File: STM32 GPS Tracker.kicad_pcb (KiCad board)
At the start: 2 copper layers, 57 parts, among them J1 Screw_Terminal_01x02, J2 LEFT HEADER PINS, J3 693010020611, J4 RIGHT HEADER PINS, Q1 AO3407A, SW1 SW_Push, SW2 SW_Push, U1 SIM808, U2 TPS5430DDA, U3 SMF05CT1G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

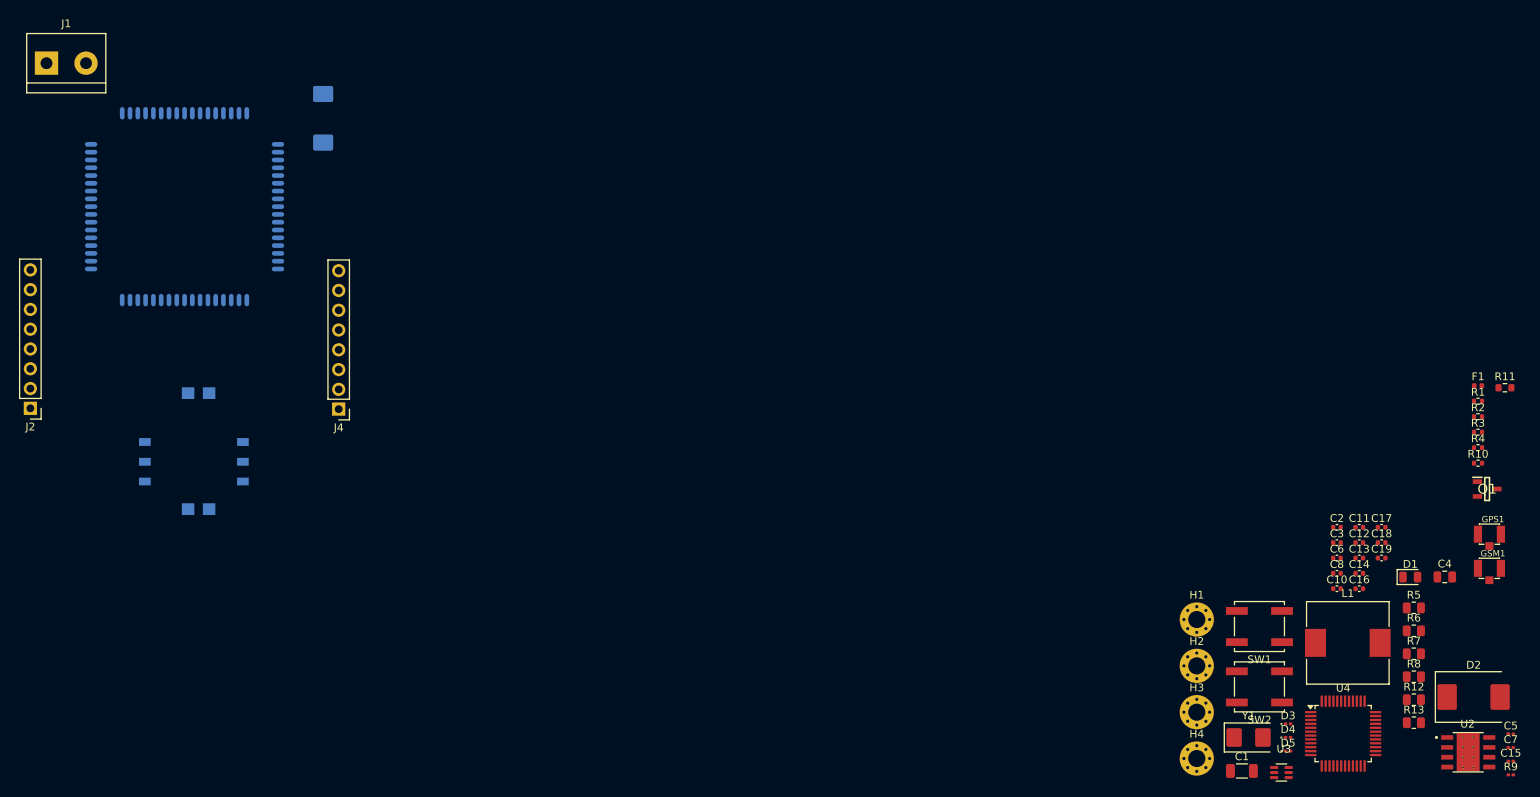
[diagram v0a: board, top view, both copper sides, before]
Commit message: Proper placing and edge cuts done for the Footprints
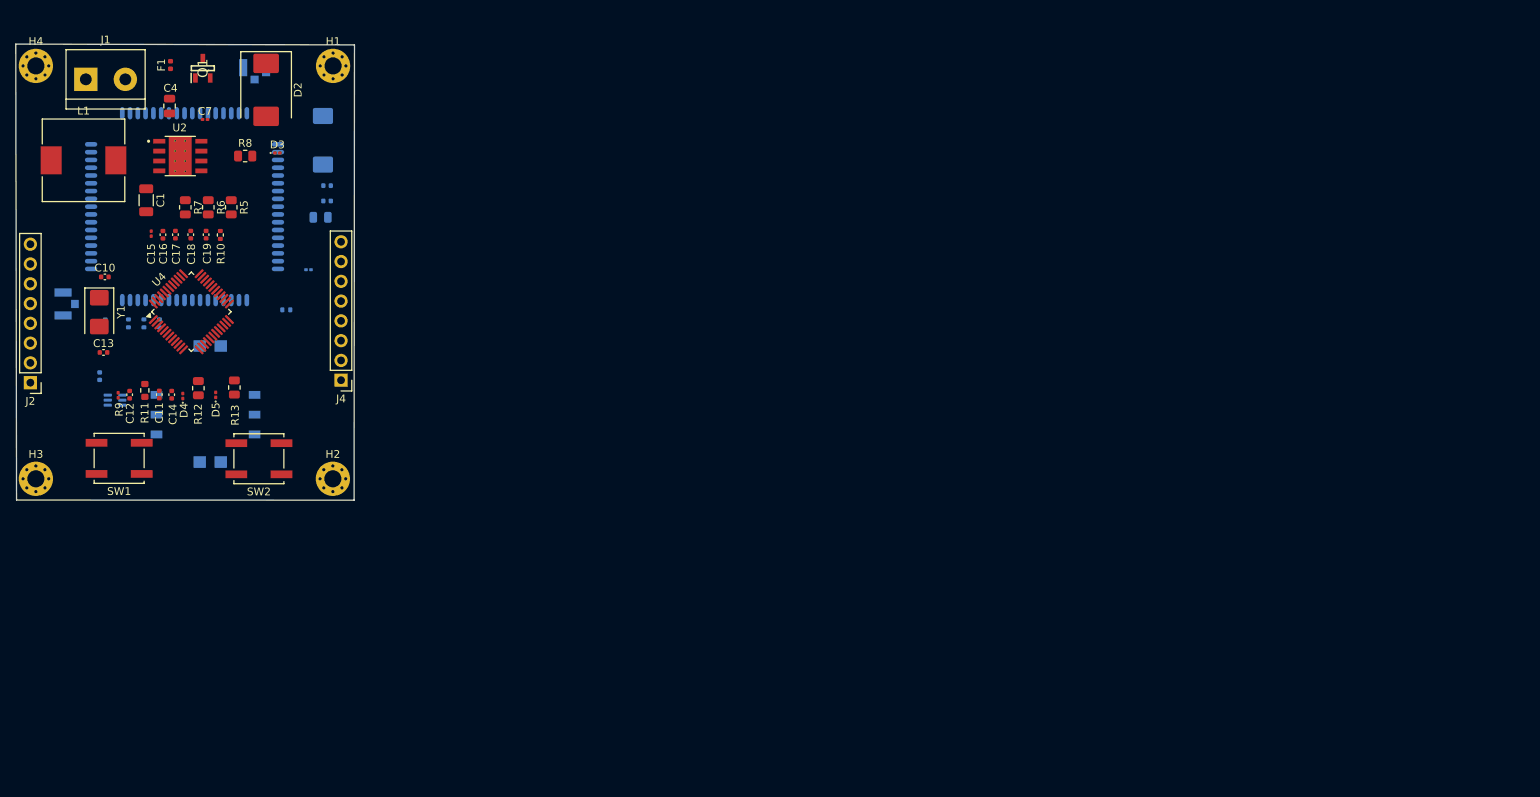
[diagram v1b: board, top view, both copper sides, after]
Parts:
- C2, C3, C5, C6, C8, D1, GPS1, GSM1, R1, R2, R3, R4, U3: moved to B.Cu
- moved C15 187.3 mm to (99.9, 89.3), turned to 90 degrees
- moved C7 186.1 mm to (106.8, 74.6)
- moved GPS1 185.6 mm to (88.6, 98.3), turned to -90 degrees
- moved R9 185.4 mm to (95.7, 110.0), turned to 90 degrees
- moved U2 182.3 mm to (103.6, 79.3)
- moved R11 174.7 mm to (99.1, 109.4), turned to -90 degrees
- moved C4 174.6 mm to (102.2, 72.9), turned to 90 degrees
- moved R4 174.1 mm to (97.0, 100.8), turned to 90 degrees
- moved L1 173.8 mm to (91.2, 79.9)
- moved H4 173.6 mm to (85.1, 67.8)
- moved D2 173.6 mm to (114.7, 70.8), turned to -90 degrees
- moved Q1 173.6 mm to (106.5, 68.0), turned to 90 degrees
- moved F1 172.9 mm to (102.4, 67.6), turned to 90 degrees
- moved R3 171.9 mm to (99.0, 100.8), turned to 90 degrees
- moved GSM1 171.1 mm to (113.2, 68.0), turned to 180 degrees
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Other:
- board outline added: 43.5 x 58.6 mm

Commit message: Round Cornering
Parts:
- moved H3 0.44 mm to (85.5, 120.8)
- moved H4 0.44 mm to (85.5, 67.8)
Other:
- board size 43.5 x 58.6 mm -> 43.5 x 58.5 mm
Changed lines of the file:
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@@
 	(footprint "MountingHole:MountingHole_2.2mm_M2_Pad_Via"
 		(layer "F.Cu")
-		(at 85.083274 67.75)
+		(at 85.525 67.75)
 		(descr "Mounting Hole 2.2mm, M2, generated by kicad-footprint-generator mountinghole.py")
 		(tags "mountinghole M2")
@@
 	(footprint "MountingHole:MountingHole_2.2mm_M2_Pad_Via"
 		(layer "F.Cu")
-		(at 85.083274 120.775)
+		(at 85.525 120.775)
 		(descr "Mounting Hole 2.2mm, M2, generated by kicad-footprint-generator mountinghole.py")
 		(tags "mountinghole M2")
@@
 	)
 	(gr_line
-		(start 126 65.05)
-		(end 125.95 123.525)
+		(start 82.6 120.75)
+		(end 82.5 67.778864)
 		(stroke
 			(width 0.05)
@@
 	)
 	(gr_line
-		(start 82.6 123.5)
-		(end 82.5 64.95)
+		(start 123.225 123.525)
+		(end 84.423767 123.501669)
+		(stroke
+			(width 0.05)
+			(type default)
+		)
+		(layer "Edge.Cuts")
+	)
+	(gr_arc
+		(start 123.325 65.05)
+		(mid 125.184437 65.85092)
+		(end 125.950467 67.725)
+		(stroke
+			(width 0.05)
+			(type default)
+		)
+		(layer "Edge.Cuts")
+	)
+	(gr_arc
+		(start 84.423767 123.501669)
+		(mid 83.090968 122.404811)
+		(end 82.6 120.75)
+		(stroke
+			(width 0.05)
+			(type default)
+		)
+		(layer "Edge.Cuts")
+	)
+	(gr_arc
+		(start 82.5 67.778864)
+		(mid 83.251232 65.921643)
+		(end 85.1 65.14984)
+		(stroke
+			(width 0.05)
+			(type default)
+		)
+		(layer "Edge.Cuts")
+	)
+	(gr_arc
+		(start 125.975 120.775)
+		(mid 125.169544 122.719544)
+		(end 123.225 123.525)
 		(stroke
 			(width 0.05)
@@
 	)
 	(gr_line
-		(start 125.95 123.525)
-		(end 82.6 123.5)
+		(start 125.950467 67.725)
+		(end 125.975 120.775)
 		(stroke
 			(width 0.05)
@@
 	)
 	(gr_line
-		(start 82.5 64.95)
-		(end 126 65.05)
+		(start 85.1 65.14984)
+		(end 123.324986 65.05)
 		(stroke
 			(width 0.05)

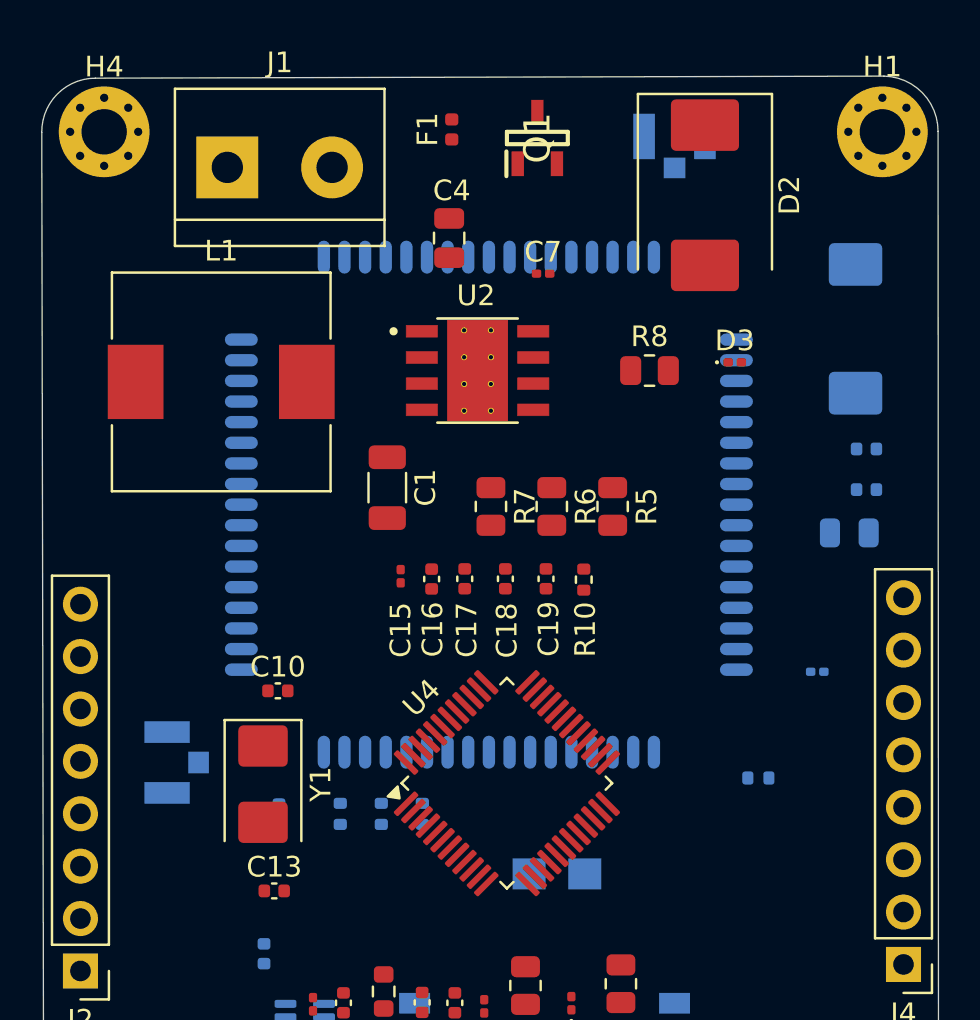
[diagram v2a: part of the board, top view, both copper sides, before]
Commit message: Routing the Top Signal Layers -Incomplete (In Progress)
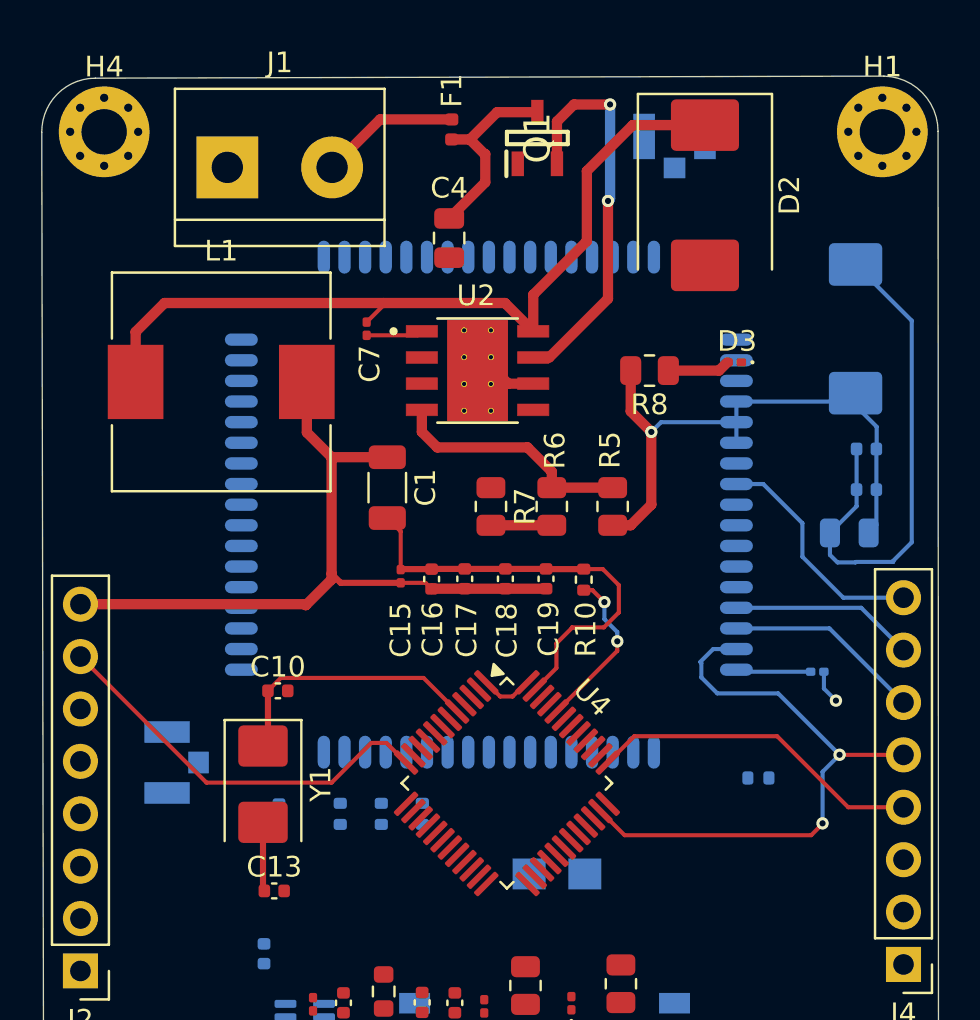
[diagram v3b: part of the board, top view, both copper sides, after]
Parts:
- moved C7 8.96 mm to (98.2, 77.3), turned to -90 degrees
- turned C4 to -90 degrees
- turned D3 to 180 degrees
- turned F1 to -90 degrees
- turned R10 to -90 degrees
- turned R5 to 90 degrees
- turned R6 to 90 degrees
- turned R8 to 180 degrees
- turned U4 to -45 degrees
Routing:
- net +3.3V: track 0.00 -> 67.6 mm, vias 0 -> 1
- net GND: track 0.00 -> 50.8 mm, vias 0 -> 1
- net Net-(D2-K): track 0.00 -> 39.6 mm
- net SIM_RESET: track 0.00 -> 29.3 mm, vias 0 -> 2
- net USART2_TX: track 0.00 -> 19.5 mm
- net Net-(Q1-S): track 0.00 -> 19.2 mm, vias 0 -> 2
- net SWDCLK: track 0.00 -> 16.3 mm
- net Net-(U4-PF0): track 0.00 -> 12.9 mm
- net FEEDBACK: track 0.00 -> 11.9 mm
- net SIM_PWRKEY: track 0.00 -> 11.3 mm
- net SIM_RX: track 0.00 -> 9.59 mm
- net Net-(Q1-D): track 0.00 -> 9.58 mm
- net SIM_TX: track 0.00 -> 8.95 mm
- net Net-(U4-BOOT0): track 0.00 -> 8.02 mm, vias 0 -> 2
- net +12V: track 0.00 -> 6.76 mm
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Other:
- copper layers 2 -> 4

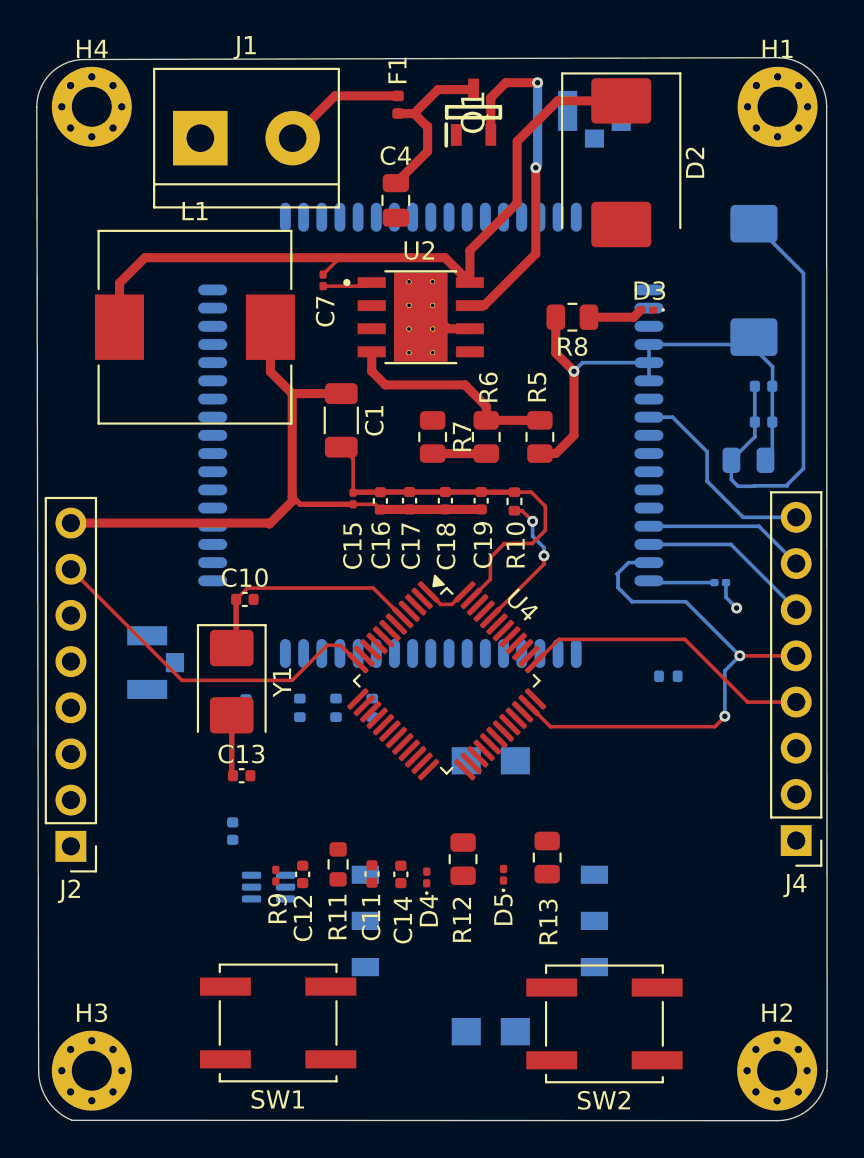
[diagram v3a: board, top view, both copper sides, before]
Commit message: Completed Tracks for Front Copper Layer
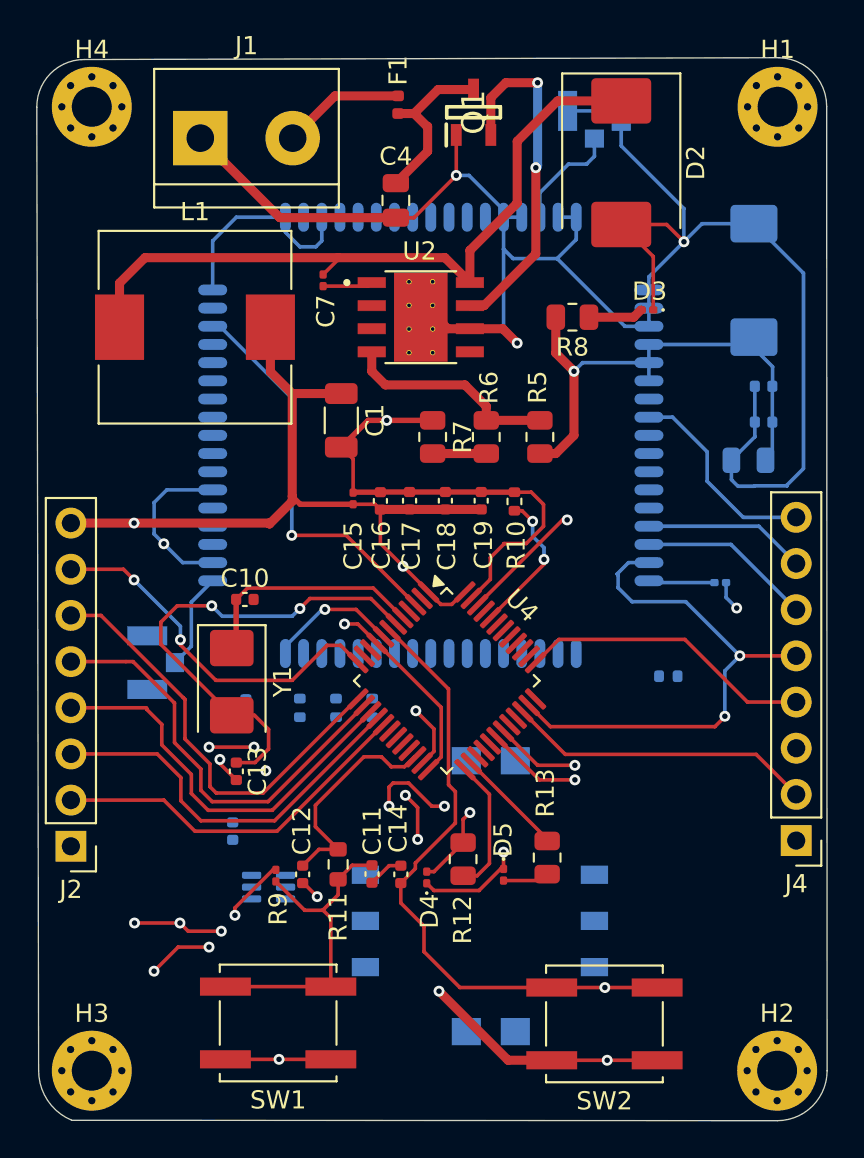
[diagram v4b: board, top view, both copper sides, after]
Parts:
- moved C13 0.38 mm to (93.5, 104.3), turned to -90 degrees
- turned C11 to -90 degrees
- turned C12 to -90 degrees
- turned C14 to -90 degrees
- turned D5 to -90 degrees
- turned R13 to -90 degrees
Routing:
- net GND: track 50.8 -> 193.9 mm, vias 1 -> 14
- net NRST: track 0.00 -> 34.6 mm, vias 0 -> 1
- net USART2_RX: track 0.00 -> 24.0 mm
- net PA4: track 0.00 -> 23.5 mm
- net Net-(U4-PF1): track 3.35 -> 26.8 mm, vias 0 -> 2
- net PA5/SPI1_CLK: track 0.00 -> 22.4 mm
- net +3.3V: track 67.6 -> 90.0 mm, vias 1 -> 5
- net STATUS: track 0.00 -> 21.9 mm, vias 0 -> 1
- net PA6/SPI1_MISO: track 0.00 -> 21.5 mm
- net PA7/SPI1_MOSI: track 0.00 -> 20.3 mm
- net (no net): track 0.00 -> 18.4 mm, vias 0 -> 12
- net Net-(C11-Pad1): track 0.00 -> 17.7 mm
- net SWDIO: track 0.00 -> 16.9 mm
- net Net-(U4-PB11): track 0.00 -> 12.3 mm
- net LED1: track 0.00 -> 7.45 mm
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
